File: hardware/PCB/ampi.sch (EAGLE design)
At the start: 41 parts, among them K1 NA, K2 NA, Q1 BSS138, U2 RASPBERRY_PI_3_MODEL_B+

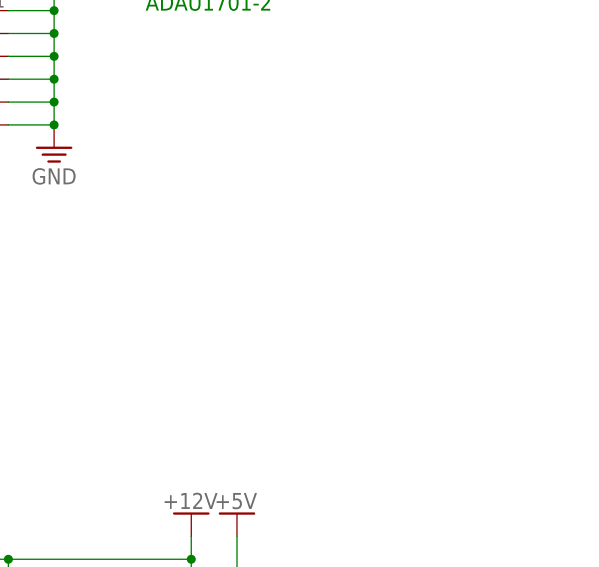
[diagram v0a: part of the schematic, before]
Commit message: fix pinout and temp_controller test
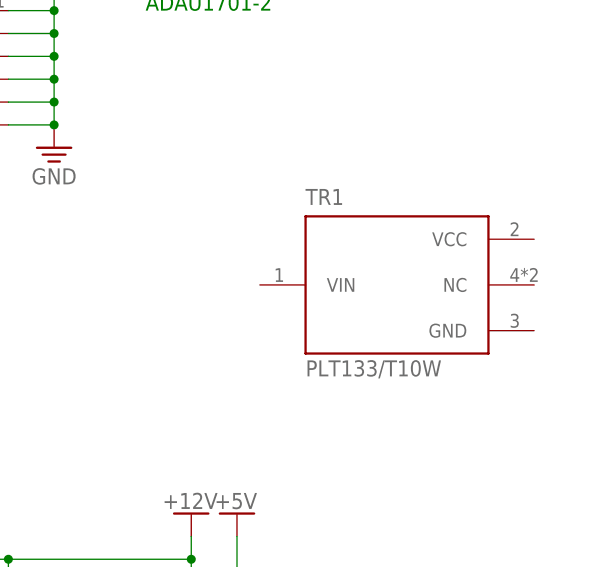
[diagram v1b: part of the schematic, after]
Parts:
- added TR1: PLT133/T10W, PLT133_T10W:PLT133/T10W
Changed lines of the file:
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@@
 <part name="PROG" library="CASE-JST" library_urn="urn:adsk.eagle:library:5637561" deviceset="PH_B6B-PH" device="" package3d_urn="urn:adsk.eagle:package:5644850/1"/>
 <part name="R15" library="Resistor" library_urn="urn:adsk.eagle:library:16378527" deviceset="R" device="CHIP-0603(1608-METRIC)" package3d_urn="urn:adsk.eagle:package:16378565/2" technology="_"/>
+<part name="TR1" library="PLT133_T10W" deviceset="PLT133/T10W" device=""/>
 </parts>
 <sheets>
@@
 <attribute name="VALUE" x="162.56" y="20.32" size="1.778" layer="95" align="center"/>
 </instance>
+<instance part="TR1" gate="G$1" x="228.6" y="-5.08" smashed="yes">
+<attribute name="NAME" x="218.44" y="3.81" size="1.778" layer="95"/>
+<attribute name="VALUE" x="218.44" y="-15.24" size="1.778" layer="96"/>
+</instance>
 </instances>
